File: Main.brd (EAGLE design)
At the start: 100 x 80 mm, 34 parts, among them IC2 74AHC1G125DBV, IC3 74AHC1G125DBV, M1 HX1, X1 BU-SMA-V

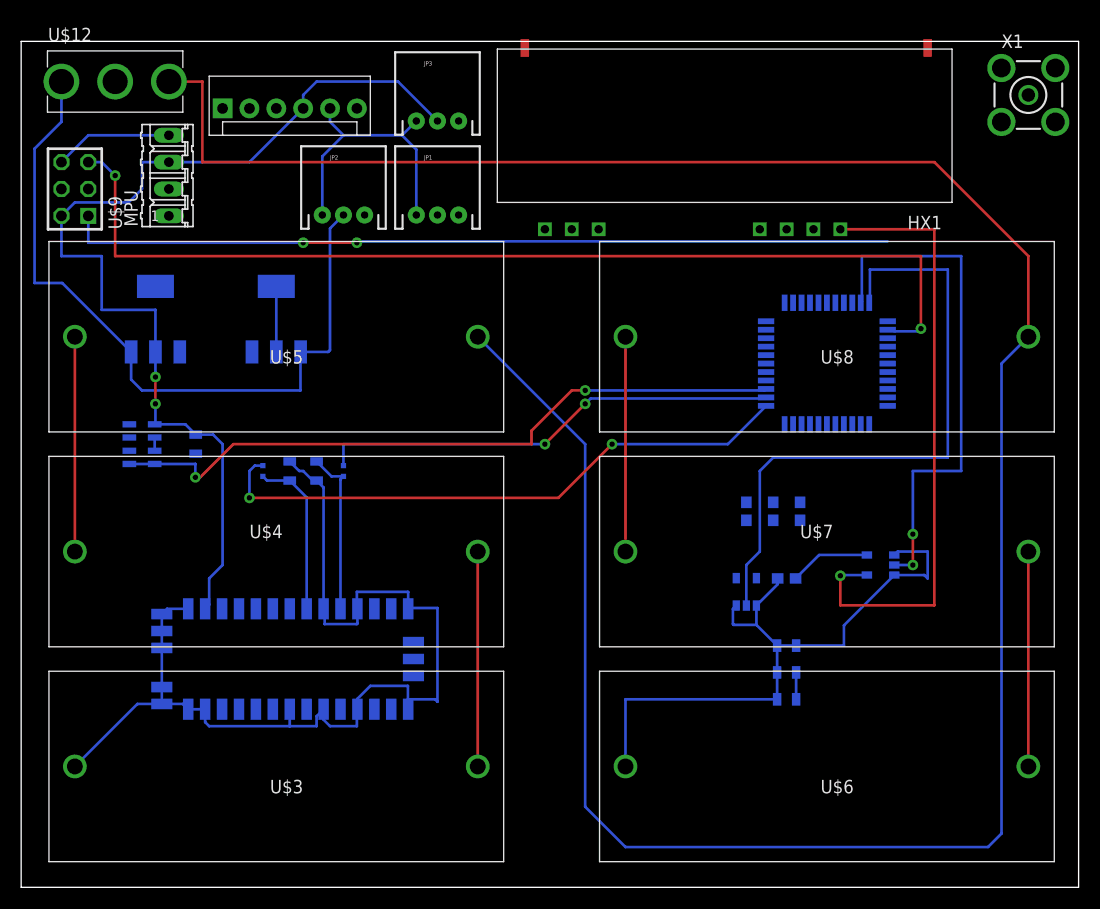
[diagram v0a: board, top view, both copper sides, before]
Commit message: Starting Board Work (caps near component they're for)
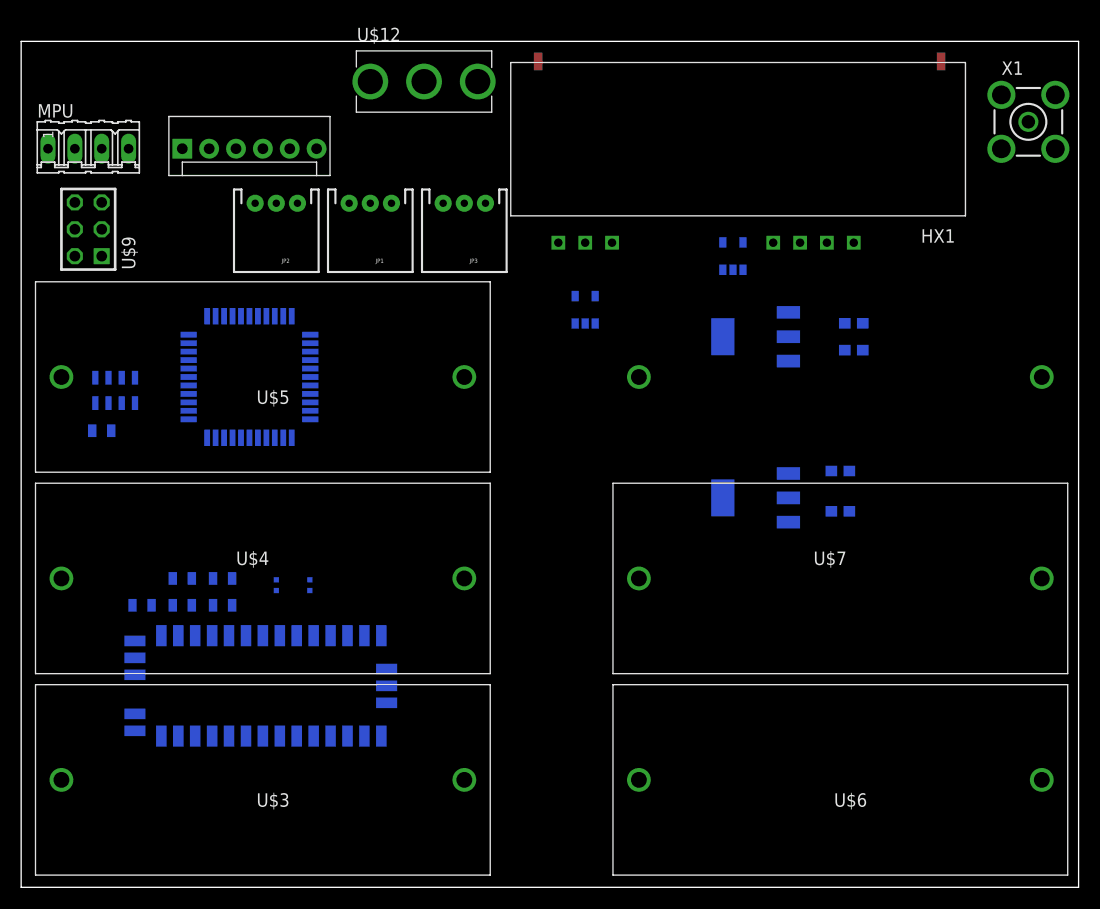
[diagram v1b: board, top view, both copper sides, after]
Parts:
- moved U$10 62.3 mm to (73.7, 36.8), turned to 270 degrees
- moved C6 61.1 mm to (11.4, 26.7), turned to 180 degrees
- moved C3 57.8 mm to (15.2, 26.7)
- moved C5 57.8 mm to (15.2, 29.2)
- moved IC1 54.6 mm to (21.6, 48.3)
- moved U$11 49.6 mm to (73.7, 52.1), turned to 270 degrees
- moved IC2 36.9 mm to (53.3, 54.6), turned to 0 degrees
- moved IC3 31.8 mm to (67.3, 59.7)
- moved U$12 29.2 mm to (38.1, 76.2)
- moved C10 25.0 mm to (78.7, 53.3)
- moved JP3 18.0 mm to (41.9, 59.7), turned to 180 degrees
- moved C9 16.1 mm to (78.7, 50.8), turned to 0 degrees
- moved C2 15.5 mm to (19.1, 26.7), turned to 0 degrees
- moved C1 12.0 mm to (19.1, 29.2), turned to 0 degrees
- moved L4 11.3 mm to (27.3, 28.6)
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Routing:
- net N$7: track 238.4 -> 0.00 mm
- net GND: track 208.7 -> 0.00 mm
- net VCC: track 99.3 -> 0.00 mm, vias 2 -> 0
- net PDI-CLK: track 96.4 -> 0.00 mm, vias 2 -> 0
- net PDI-DATA: track 78.2 -> 0.00 mm, vias 2 -> 0
- net BATT: track 70.8 -> 0.00 mm
- net SSC: track 65.7 -> 0.00 mm, vias 2 -> 0
- net TXE: track 59.9 -> 0.00 mm
- net TXD-5V: track 58.7 -> 0.00 mm, vias 1 -> 0
- net RXC: track 56.5 -> 0.00 mm, vias 2 -> 0
- net RXE: track 49.4 -> 0.00 mm, vias 2 -> 0
- net TXC: track 43.8 -> 0.00 mm, vias 2 -> 0
- net N$9: track 20.3 -> 0.00 mm
- net N$8: track 20.3 -> 0.00 mm
- net N$6: track 20.3 -> 0.00 mm
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
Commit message: Rev1. of Board Done
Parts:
- moved IC2 30.2 mm to (82.5, 62.2), turned to 270 degrees
- moved C5 20.5 mm to (25.4, 11.4), turned to 180 degrees
- moved C9 16.1 mm to (63.5, 45.7), turned to 90 degrees
- moved C10 15.7 mm to (63.5, 49.5), turned to 270 degrees
- moved C4 14.2 mm to (63.5, 41.9), turned to 90 degrees
- moved C8 14.2 mm to (63.5, 38.1), turned to 270 degrees
- moved C2 9.55 mm to (28.6, 26.0), turned to 180 degrees
- moved U$11 8.52 mm to (66.0, 48.3), turned to 90 degrees
- moved U$10 8.03 mm to (66.0, 39.4), turned to 90 degrees
- moved C6 6.35 mm to (7.62, 21.6), turned to 270 degrees
- moved C1 5.46 mm to (23.5, 26.0)
- moved C7 3.17 mm to (5.71, 45.7), turned to 90 degrees
- moved C3 1.27 mm to (14.0, 26.7)
- moved L3 0.64 mm to (24.8, 28.6)
- moved L4 0.64 mm to (27.9, 28.6)
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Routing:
- net GND: track 0.00 -> 412.2 mm, vias 0 -> 3
- net VCC: track 0.00 -> 261.0 mm, vias 0 -> 9
- net N$7: track 0.00 -> 122.0 mm, vias 0 -> 3
- net BATT: track 0.00 -> 90.0 mm, vias 0 -> 1
- net RXE: track 0.00 -> 75.2 mm, vias 0 -> 4
- net RXD: track 0.00 -> 60.0 mm
- net TXD: track 0.00 -> 57.0 mm, vias 0 -> 2
- net N$5: track 0.00 -> 45.4 mm
- net GC2: track 0.00 -> 44.3 mm, vias 0 -> 2
- net TXE: track 0.00 -> 43.3 mm, vias 0 -> 2
- net PDI-CLK: track 0.00 -> 39.3 mm, vias 0 -> 1
- net SCLKD: track 0.00 -> 34.3 mm
- net SDID: track 0.00 -> 32.7 mm, vias 0 -> 1
- net TXC: track 0.00 -> 28.7 mm, vias 0 -> 4
- net THERM: track 0.00 -> 28.4 mm, vias 0 -> 2
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
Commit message: Added Silkscreen
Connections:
- net GND: now also M1.BODYGND1, M1.BODYGND2
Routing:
- net GND: track 412.2 -> 459.6 mm
- added copper zone on layer 1, net GND
- added copper zone on layer 16, net GND
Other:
- board text added: "/storage/Chrome/croc.bmp"
- board text added: "100nF"
- board text added: "18pF"
- board text added: "1uF"
- board text added: "22pF"
- board text added: "22uF"
- board text added: "3.3V"
- board text added: "47uF"
- board text added: "5V"
- board text added: "ANT"
- board text added: "BATT"
- board text added: "FB"
- board text added: "GC1"
- board text added: "GC2"
- board text added: "GND"
- board text added: "GPS"
- board text added: "LOGIC"
- board text added: "MPU-9250"
- board text added: "MS5607"
- board text added: "OPEN-LOG"
- board text added: "PDI"
- board text added: "Physoon 2.0"
- board text added: "RBF"
- board text added: "Radio"
- board text added: "Therm"
